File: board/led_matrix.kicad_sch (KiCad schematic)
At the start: 0 parts

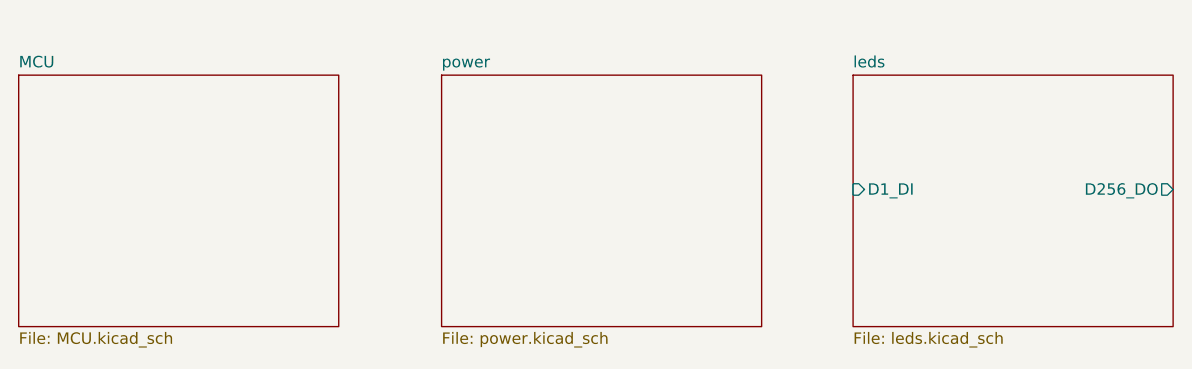
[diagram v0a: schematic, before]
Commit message: Finished everything except assigning footprints for passives
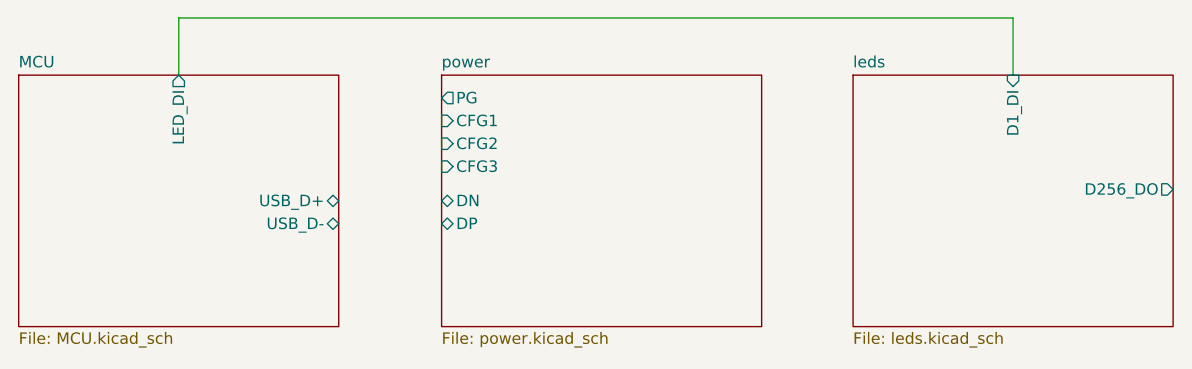
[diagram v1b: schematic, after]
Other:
- sheet MCU ports: added LED_DI, USB_D+, USB_D-; removed none
- sheet power ports: added CFG1, CFG2, CFG3, DN, DP, PG; removed none
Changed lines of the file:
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@@
 	(generator_version "9.0")
 	(paper "A4")
+	(wire
+		(pts
+			(xy 91.44 72.39) (xy 184.15 72.39)
+		)
+		(stroke
+			(width 0)
+			(type default)
+		)
+	)
+	(wire
+		(pts
+			(xy 91.44 78.74) (xy 91.44 72.39)
+		)
+		(stroke
+			(width 0)
+			(type default)
+		)
+	)
+	(wire
+		(pts
+			(xy 184.15 72.39) (xy 184.15 78.74)
+		)
+		(stroke
+			(width 0)
+			(type default)
+		)
+	)
 	(sheet
 		(at 166.37 78.74)
@@
 		)
 		(pin "D1_DI" input
-			(at 166.37 91.44 180)
-			(effects
-				(font
-					(size 1.27 1.27)
-				)
-				(justify left)
+			(at 184.15 78.74 90)
+			(effects
+				(font
+					(size 1.27 1.27)
+				)
+				(justify right)
 			)
 		)
@@
 			)
 		)
+		(pin "USB_D+" bidirectional
+			(at 109.22 92.71 0)
+			(effects
+				(font
+					(size 1.27 1.27)
+				)
+				(justify right)
+			)
+		)
+		(pin "USB_D-" bidirectional
+			(at 109.22 95.25 0)
+			(effects
+				(font
+					(size 1.27 1.27)
+				)
+				(justify right)
+			)
+		)
+		(pin "LED_DI" output
+			(at 91.44 78.74 90)
+			(effects
+				(font
+					(size 1.27 1.27)
+				)
+				(justify right)
+			)
+		)
 		(instances
 			(project "led_matrix"
@@
 			)
 		)
+		(pin "CFG1" input
+			(at 120.65 83.82 180)
+			(effects
+				(font
+					(size 1.27 1.27)
+				)
+				(justify left)
+			)
+		)
+		(pin "CFG2" input
+			(at 120.65 86.36 180)
+			(effects
+				(font
+					(size 1.27 1.27)
+				)
+				(justify left)
+			)
+		)
+		(pin "CFG3" input
+			(at 120.65 88.9 180)
+			(effects
+				(font
+					(size 1.27 1.27)
+				)
+				(justify left)
+			)
+		)
+		(pin "DN" bidirectional
+			(at 120.65 92.71 180)
+			(effects
+				(font
+					(size 1.27 1.27)
+				)
+				(justify left)
+			)
+		)
+		(pin "DP" bidirectional
+			(at 120.65 95.25 180)
+			(effects
+				(font
+					(size 1.27 1.27)
+				)
+				(justify left)
+			)
+		)
+		(pin "PG" output
+			(at 120.65 81.28 180)
+			(effects
+				(font
+					(size 1.27 1.27)
+				)
+				(justify left)
+			)
+		)

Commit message: Added footprints for everything except buck inductor and resistor
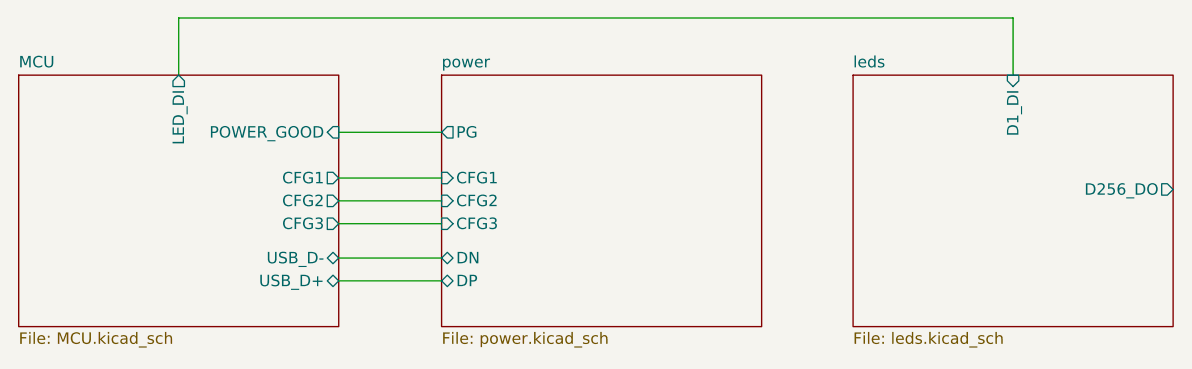
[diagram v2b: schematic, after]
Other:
- sheet MCU ports: added CFG1, CFG2, CFG3, POWER_GOOD; removed none
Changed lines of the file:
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@@
+	(wire
+		(pts
+			(xy 109.22 99.06) (xy 120.65 99.06)
+		)
+		(stroke
+			(width 0)
+			(type default)
+		)
+	)
 	(wire
 		(pts
@@
 	(wire
 		(pts
+			(xy 109.22 101.6) (xy 120.65 101.6)
+		)
+		(stroke
+			(width 0)
+			(type default)
+		)
+	)
+	(wire
+		(pts
+			(xy 109.22 95.25) (xy 120.65 95.25)
+		)
+		(stroke
+			(width 0)
+			(type default)
+		)
+	)
+	(wire
+		(pts
+			(xy 109.22 85.09) (xy 120.65 85.09)
+		)
+		(stroke
+			(width 0)
+			(type default)
+		)
+	)
+	(wire
+		(pts
+			(xy 109.22 90.17) (xy 120.65 90.17)
+		)
+		(stroke
+			(width 0)
+			(type default)
+		)
+	)
+	(wire
+		(pts
 			(xy 91.44 78.74) (xy 91.44 72.39)
 		)
@@
 		(pts
 			(xy 184.15 72.39) (xy 184.15 78.74)
+		)
+		(stroke
+			(width 0)
+			(type default)
+		)
+	)
+	(wire
+		(pts
+			(xy 109.22 92.71) (xy 120.65 92.71)
 		)
 		(stroke
@@
 		)
 		(pin "USB_D+" bidirectional
-			(at 109.22 92.71 0)
+			(at 109.22 101.6 0)
 			(effects
 				(font
@@
 		)
 		(pin "USB_D-" bidirectional
-			(at 109.22 95.25 0)
+			(at 109.22 99.06 0)
 			(effects
 				(font
@@
 		(pin "LED_DI" output
 			(at 91.44 78.74 90)
+			(effects
+				(font
+					(size 1.27 1.27)
+				)
+				(justify right)
+			)
+		)
+		(pin "CFG1" output
+			(at 109.22 90.17 0)
+			(effects
+				(font
+					(size 1.27 1.27)
+				)
+				(justify right)
+			)
+		)
+		(pin "CFG2" output
+			(at 109.22 92.71 0)
+			(effects
+				(font
+					(size 1.27 1.27)
+				)
+				(justify right)
+			)
+		)
+		(pin "CFG3" output
+			(at 109.22 95.25 0)
+			(effects
+				(font
+					(size 1.27 1.27)
+				)
+				(justify right)
+			)
+		)
+		(pin "POWER_GOOD" input
+			(at 109.22 85.09 0)
 			(effects
 				(font
@@
 		)
 		(pin "CFG1" input
-			(at 120.65 83.82 180)
+			(at 120.65 90.17 180)
 			(effects
 				(font
@@
 		)
 		(pin "CFG2" input
-			(at 120.65 86.36 180)
+			(at 120.65 92.71 180)
 			(effects
 				(font
@@
 		)
 		(pin "CFG3" input
-			(at 120.65 88.9 180)
+			(at 120.65 95.25 180)
 			(effects
 				(font
@@
 		)
 		(pin "DN" bidirectional
-			(at 120.65 92.71 180)
+			(at 120.65 99.06 180)
 			(effects
 				(font
@@
 		)
 		(pin "DP" bidirectional
-			(at 120.65 95.25 180)
+			(at 120.65 101.6 180)
 			(effects
 				(font
@@
 		)
 		(pin "PG" output
-			(at 120.65 81.28 180)
-			(effects
-				(font
+			(at 120.65 85.09 180)
+			(effects
+				(font

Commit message: Routed usb diff pair
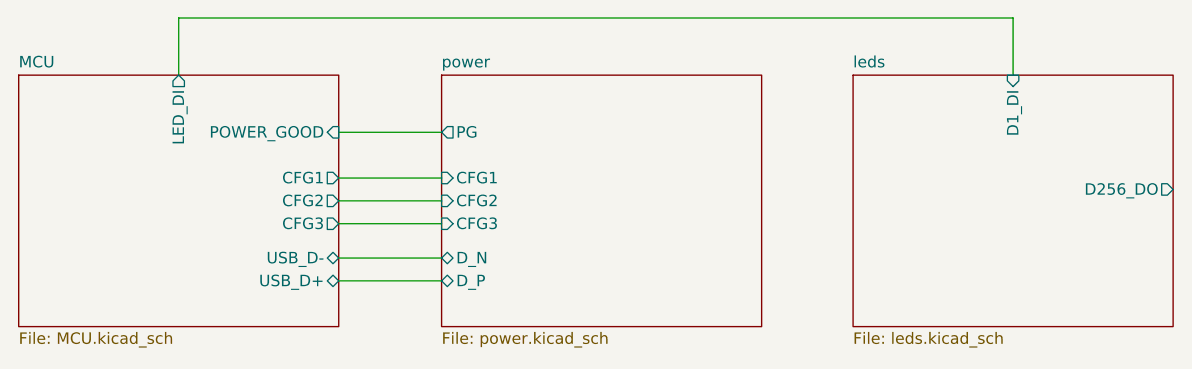
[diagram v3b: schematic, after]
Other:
- sheet power ports: added D_N, D_P; removed DN, DP
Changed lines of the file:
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@@
 			)
 		)
-		(pin "DN" bidirectional
+		(pin "PG" output
+			(at 120.65 85.09 180)
+			(effects
+				(font
+					(size 1.27 1.27)
+				)
+				(justify left)
+			)
+		)
+		(pin "D_N" bidirectional
 			(at 120.65 99.06 180)
 			(effects
@@
 			)
 		)
-		(pin "DP" bidirectional
+		(pin "D_P" bidirectional
 			(at 120.65 101.6 180)
 			(effects
 				(font
-					(size 1.27 1.27)
-				)
-				(justify left)
-			)
-		)
-		(pin "PG" output
-			(at 120.65 85.09 180)
-			(effects
-				(font
